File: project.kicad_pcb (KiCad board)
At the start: 2 copper layers, 114.3 x 48.3 mm, 31 parts, among them J1 Conn_01x02, J2 Conn_01x15, J3 Conn_01x15, J4 Conn_01x02, J5 Conn_01x02, J6 Conn_01x02, U1 DRV8870DDA, U2 DRV8870DDA, U3 DRV8870DDA

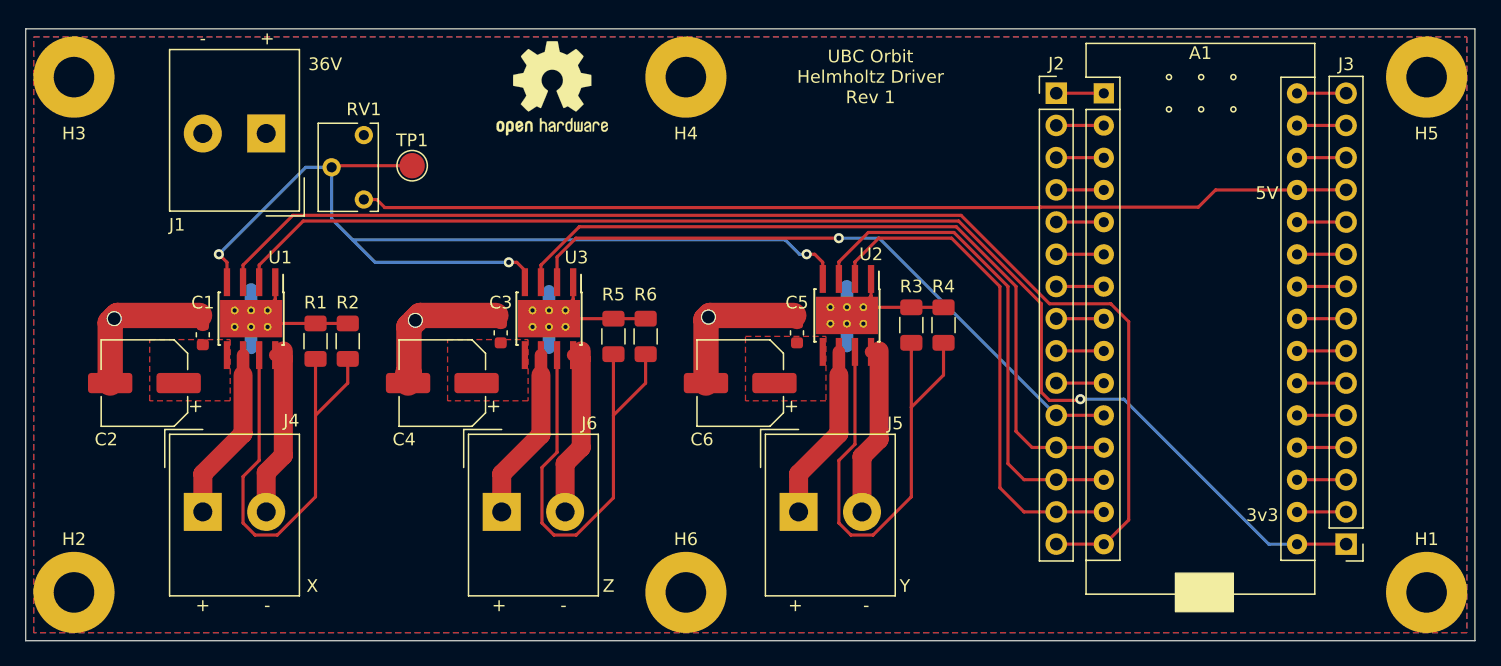
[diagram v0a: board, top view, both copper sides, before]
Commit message: Shorten board width
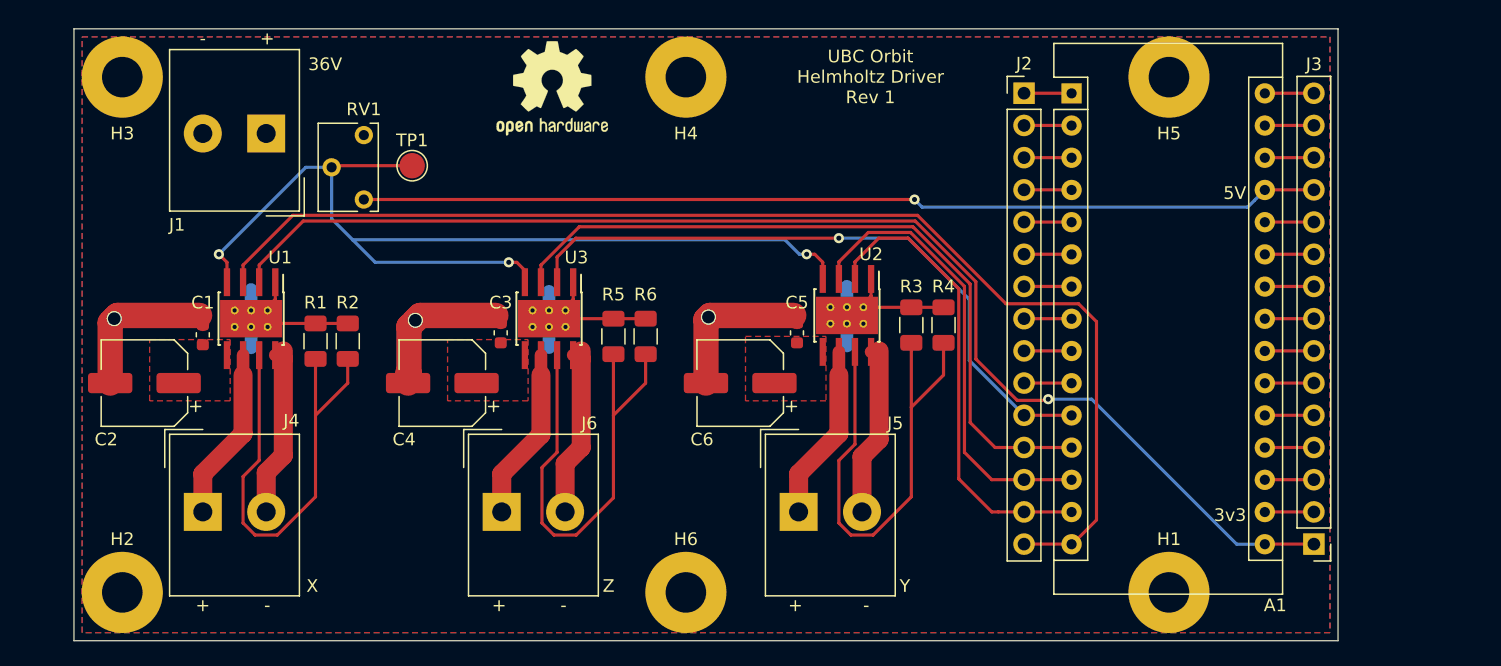
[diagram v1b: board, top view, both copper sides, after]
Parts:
- moved H1 20.3 mm to (129.5, 149.9)
- moved H5 20.3 mm to (129.5, 109.2)
- moved H2 3.81 mm to (47.0, 149.9)
- moved H3 3.81 mm to (47.0, 109.2)
- moved A1 2.54 mm to (121.9, 110.5)
- moved J2 2.54 mm to (118.1, 110.5)
- moved J3 2.54 mm to (141.0, 146.1)
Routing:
- net IN_Y_2: track 40.1 -> 37.0 mm
- net IN_X_2: track 103.2 -> 100.1 mm
- net IN_Y_1: track 39.5 -> 36.5 mm
- net IN_Z_1: track 61.0 -> 58.1 mm
- net +5V: track 78.2 -> 75.7 mm, vias 0 -> 1
- net IN_X_1: track 98.4 -> 95.9 mm
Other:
- board size 114.3 x 48.3 mm -> 99.7 x 48.3 mm
